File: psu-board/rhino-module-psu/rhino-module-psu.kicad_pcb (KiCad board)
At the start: 2 copper layers, 225.4 x 35 mm, 26 parts, among them IC1 78T

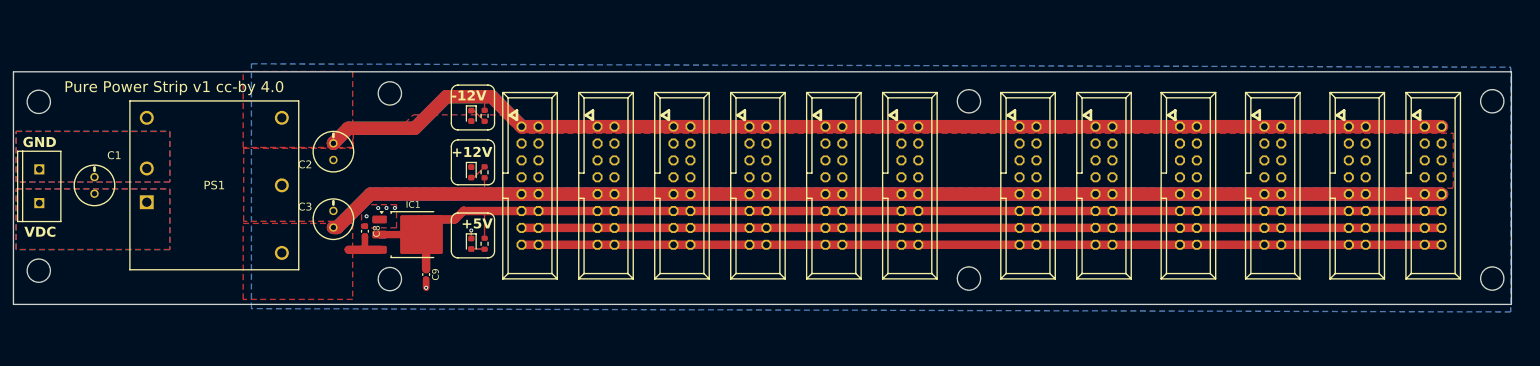
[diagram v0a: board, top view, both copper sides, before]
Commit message: Added HSUSB datasheet
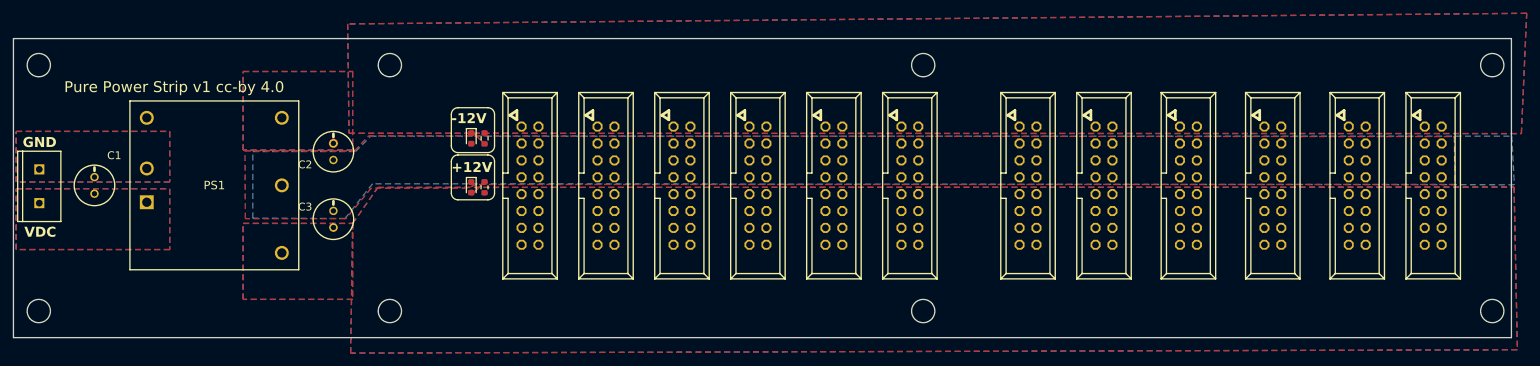
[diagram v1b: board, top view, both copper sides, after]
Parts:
- removed C8, C9: C-US025-024X044, Capacitor_SMD:C_0603_1608Metric
- removed D2: LED, LED_SMD:LED_0603_1608Metric
- removed IC1: 78T, Package_TO_SOT_SMD:TO-252-3_TabPin2
- removed R3: R-US_0207/10, Resistor_SMD:R_0603_1608Metric
- moved D3 3.41 mm to (106.0, 90.0)
- moved R2 3.41 mm to (108.0, 90.0)
- moved D1 2.26 mm to (106.0, 97.4)
- moved R1 2.26 mm to (108.0, 97.4)
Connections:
- U$10 pad +5: +5V -> +12V
- U$10 pad +5A: +5V -> +12V
- U$10 pad CV: /CV2 -> +12V
- U$10 pad CVA: /CV2 -> +12V
- U$10 pad GATE: /CV1 -> +12V
- U$10 pad GATEA: /CV1 -> +12V
- U$11 pad +5: +5V -> +12V
- U$11 pad +5A: +5V -> +12V
- U$11 pad CV: /CV2 -> +12V
- U$11 pad CVA: /CV2 -> +12V
- U$11 pad GATE: /CV1 -> +12V
- U$11 pad GATEA: /CV1 -> +12V
- U$12 pad +5: +5V -> +12V
- U$12 pad +5A: +5V -> +12V
- U$12 pad CV: /CV2 -> +12V
- U$12 pad CVA: /CV2 -> +12V
- U$12 pad GATE: /CV1 -> +12V
- U$12 pad GATEA: /CV1 -> +12V
- U$13 pad +5: +5V -> +12V
- U$13 pad +5A: +5V -> +12V
- U$13 pad CV: /CV2 -> +12V
- U$13 pad CVA: /CV2 -> +12V
- U$13 pad GATE: /CV1 -> +12V
- U$13 pad GATEA: /CV1 -> +12V
- U$2 pad +5: +5V -> +12V
- U$2 pad +5A: +5V -> +12V
- U$2 pad CV: /CV2 -> +12V
- U$2 pad CVA: /CV2 -> +12V
- U$2 pad GATE: /CV1 -> +12V
- U$2 pad GATEA: /CV1 -> +12V
- U$3 pad +5: +5V -> +12V
- U$3 pad +5A: +5V -> +12V
- U$3 pad CV: /CV2 -> +12V
- U$3 pad CVA: /CV2 -> +12V
- U$3 pad GATE: /CV1 -> +12V
- U$3 pad GATEA: /CV1 -> +12V
- U$4 pad +5: +5V -> +12V
- U$4 pad +5A: +5V -> +12V
- U$4 pad CV: /CV2 -> +12V
- U$4 pad CVA: /CV2 -> +12V
- U$4 pad GATE: /CV1 -> +12V
- U$4 pad GATEA: /CV1 -> +12V
- U$5 pad +5: +5V -> +12V
- U$5 pad +5A: +5V -> +12V
- U$5 pad CV: /CV2 -> +12V
- U$5 pad CVA: /CV2 -> +12V
- U$5 pad GATE: /CV1 -> +12V
- U$5 pad GATEA: /CV1 -> +12V
- U$6 pad +5: +5V -> +12V
- U$6 pad +5A: +5V -> +12V
- U$6 pad CV: /CV2 -> +12V
- U$6 pad CVA: /CV2 -> +12V
- U$6 pad GATE: /CV1 -> +12V
- U$6 pad GATEA: /CV1 -> +12V
- U$7 pad +5: +5V -> +12V
- U$7 pad +5A: +5V -> +12V
- U$7 pad CV: /CV2 -> +12V
- U$7 pad CVA: /CV2 -> +12V
- U$7 pad GATE: /CV1 -> +12V
- U$7 pad GATEA: /CV1 -> +12V
- U$8 pad +5: +5V -> +12V
- U$8 pad +5A: +5V -> +12V
- U$8 pad CV: /CV2 -> +12V
- U$8 pad CVA: /CV2 -> +12V
- U$8 pad GATE: /CV1 -> +12V
- U$8 pad GATEA: /CV1 -> +12V
- U$9 pad +5: +5V -> +12V
- U$9 pad +5A: +5V -> +12V
- U$9 pad CV: /CV2 -> +12V
- U$9 pad CVA: /CV2 -> +12V
- U$9 pad GATE: /CV1 -> +12V
- U$9 pad GATEA: /CV1 -> +12V
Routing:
- net +12V: track 346.7 -> 0.08 mm
- net -12V: track 206.2 -> 0.03 mm
- net +5V: track 173.1 -> 0.00 mm
- net /CV1: track 138.5 -> 0.00 mm
- net /CV2: track 138.4 -> 0.00 mm
- net GND: track 2.44 -> 0.39 mm, vias 6 -> 0
- net Net-(D2-A): track 1.96 -> 0.00 mm
- added copper zone on B.Cu, net +12V
- added copper zone on B.Cu, net -12V
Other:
- board size 225.4 x 35 mm -> 225.4 x 45 mm
- board text removed: "+5V"
